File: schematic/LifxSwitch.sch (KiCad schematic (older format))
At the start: 27 parts

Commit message: Completed Schematic
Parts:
- removed C?: 4.7uF, symbol C
- removed L?: 3.3uH, symbol L
- removed R?: 50k, symbol R
- removed R?: 25k, symbol R
- removed U?: ST1S06, symbol ST1S06
- added C1, C3: 4.7uF, symbol C
- added C2, C4: 0.1uF, symbol C
- added D1: SP0503BAHTG, SOT192P237X122-4N, symbol SP0503BAHTG
- added D2, D3: LED, symbol LED
- added J4: CP2102, symbol Conn_01x02
- added J5: Arcade, symbol Conn_01x01
- added R1: 1k, symbol R
- added R2: 22.1k, symbol R
- added R3: 47.5k, symbol R
- added U2: CP2102N-A01-GQFN20, SILABS_QFN20, symbol CP2102N-A01-GQFN20
- gave numbers to parts that had none: 22
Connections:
- net +3V3: now also R4.1, C1.2, C2.2, D2.2 (A), D3.2 (A), R1.1, U2.6 (VDD)
- net +5V: now also C3.2, C4.2, D1.3 (B), R2.1, U2.7 (VREGIN)
- net LightStatus: now also J5.1 (Pin_1)
- net RX: now also U2.18 (TXD)
- net TX: now also U2.17 (RXD)
- net VSS: now also C7.1, C8.1, J3.5 (Shield), C1.1, C2.1, C3.1, C4.1, D1.1 (GND), R3.2, U2.12 (GND), U2.21 (GND), U2.3 (GND)
- net Gpio0: now reaches U3.8 (RDY), U4.12 (GPIO0)
- net at J3.2 (D-): now also D1.2 (A), U2.5 (D)
- net at J3.3 (D+): now also D1.4 (C), U2.4 (D+)
- new net: D2.1 (K), U2.19 (GPIO.3/RXT)
- new net: D3.1 (K), U2.20 (GPIO.2/TXT)
- new net: R2.2, R3.1, U2.8 (VBUS)
- new net: R1.2, U2.9 (RST)
- new net G0: J4.1 (Pin_1), U2.2 (GPIO.0/CLK)
- new net G1: J4.2 (Pin_2), U2.1 (GPIO.1/RS485)
- no-connect marks 2 -> 15
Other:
- moved on the sheet: C5, C6, C7, C8, C9, D4, D5, D6, D7, J3, R10, R4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

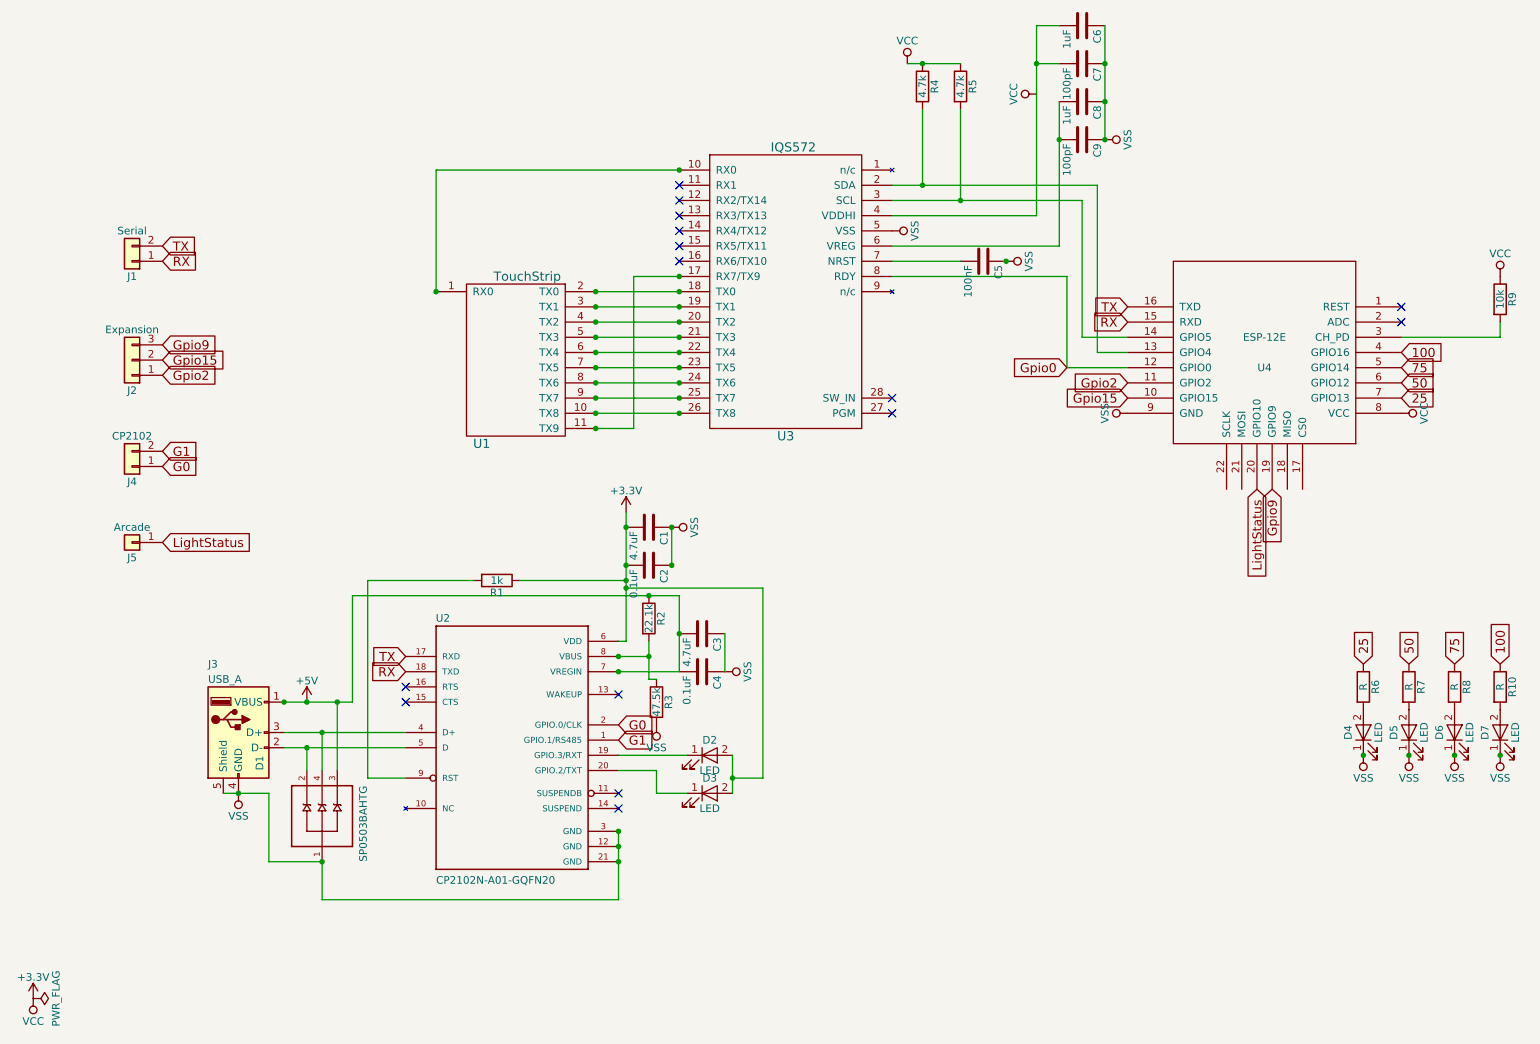
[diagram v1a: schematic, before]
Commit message: Completed PCB layout
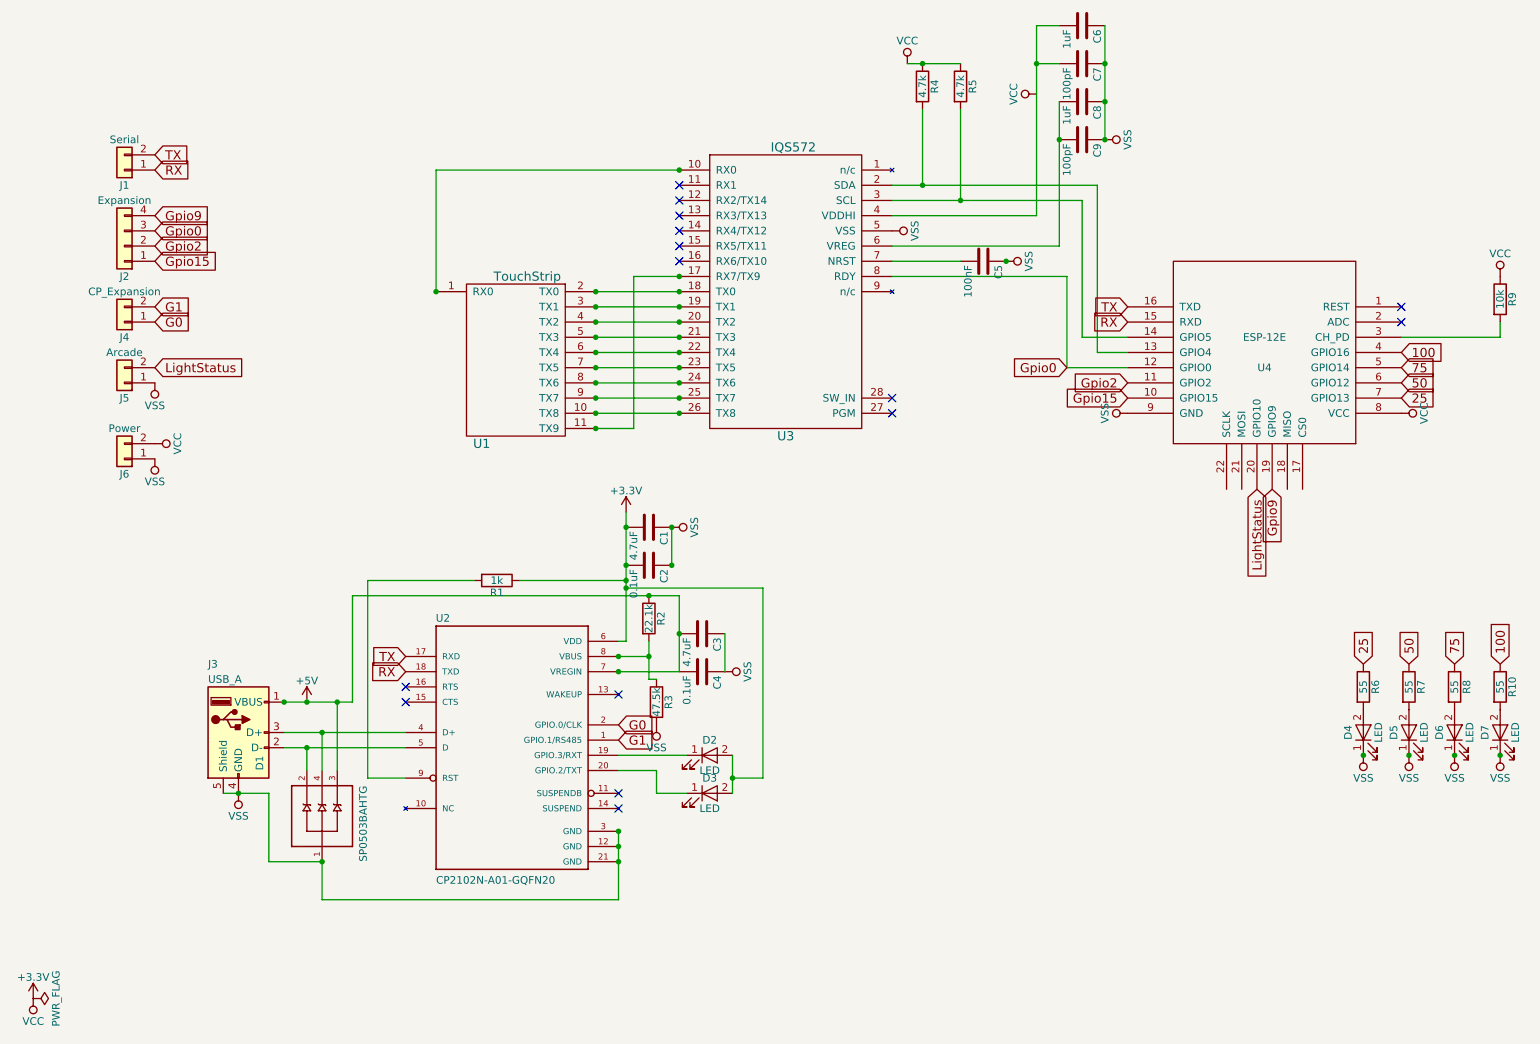
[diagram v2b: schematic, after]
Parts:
- removed J2: Expansion, symbol Conn_01x03
- removed J5: Arcade, symbol Conn_01x01
- added J2: Expansion, Pin_Headers:Pin_Header_Straight_1x04_Pitch2.54mm, symbol Conn_01x04
- added J5: Arcade, Pin_Headers:Pin_Header_Straight_1x02_Pitch2.54mm, symbol Conn_01x02
- added J6: Power, Pin_Headers:Pin_Header_Straight_1x02_Pitch2.54mm, symbol Conn_01x02
- C1, C2, C3, C4, C5, C6, C7, C8, C9: footprint (none) -> Capacitors_SMD:C_0805
- D1: footprint SOT192P237X122-4N -> SP0503BAHTG:SOT192P237X122-4N
- D2, D3, D4, D5, D6, D7: footprint (none) -> LEDs:LED_0805
- J1: footprint (none) -> Pin_Headers:Pin_Header_Straight_1x02_Pitch2.54mm
- J3: footprint (none) -> Connectors_USB:USB_Micro-B_Molex_47346-0001
- J4: value CP2102 -> CP_Expansion; footprint (none) -> Pin_Headers:Pin_Header_Straight_1x02_Pitch2.54mm
- R1, R2, R3, R4, R5, R9: footprint (none) -> Resistors_SMD:R_0805
- R10, R6, R7, R8: value R -> 55; footprint (none) -> Resistors_SMD:R_0805
- U1: footprint (none) -> Buttons_Switches_SMD:Touchstrip
- U2: footprint SILABS_QFN20 -> CP2102N-A01-GQFN20:SILABS_QFN20
- U3: footprint (none) -> Housings_DFN_QFN:QFN-28-1EP_4x4mm_Pitch0.4mm-Without-Center-Pads
- U4: footprint (none) -> ESP8266:ESP-12E
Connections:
- net +3V3: now also J6.2 (Pin_2)
- net Gpio0: now also J2.3 (Pin_3)
- net Gpio15: now also J2.1 (Pin_1)
- net Gpio2: now also J2.2 (Pin_2)
- net Gpio9: now also J2.4 (Pin_4)
- net LightStatus: now also J5.2 (Pin_2)
- net VSS: now also J5.1 (Pin_1), J6.1 (Pin_1)
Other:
- moved on the sheet: J1, J4

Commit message: Finished V1 schematic
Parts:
- removed J5: Arcade, Pin_Headers:Pin_Header_Straight_1x02_Pitch2.54mm, symbol Conn_01x02
- added C10: 10uF, symbol C
- added C11: 0.1uF, symbol C
- added J5: Arcade, Pin_Headers:Pin_Header_Straight_1x04_Pitch2.54mm, symbol Conn_01x04
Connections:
- net +3V3: now also C10.1, C11.1
- net Gpio15: now also J5.3 (Pin_3)
- net LightStatus: now also J5.4 (Pin_4)
- net VSS: now also C10.2, C11.2, J5.1 (Pin_1), J5.2 (Pin_2)
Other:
- moved on the sheet: J6
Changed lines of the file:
@@
 L VCC #PWR09
 U 1 1 5B29EAF7
-P 10050 3300
-F 0 "#PWR09" H 10050 3150 50  0001 C CNN
-F 1 "VCC" H 10050 3450 50  0000 C CNN
-F 2 "" H 10050 3300 50  0001 C CNN
-F 3 "" H 10050 3300 50  0001 C CNN
-	1    10050 3300
+P 10400 3300
+F 0 "#PWR09" H 10400 3150 50  0001 C CNN
+F 1 "VCC" H 10400 3450 50  0000 C CNN
+F 2 "" H 10400 3300 50  0001 C CNN
+F 3 "" H 10400 3300 50  0001 C CNN
+	1    10400 3300
 	0    1    1    0
 $EndComp
@@
 Connection ~ 3700 2500
 Connection ~ 5300 1700
-Text GLabel 1850 3000 2    60   Input ~ 0
+Text GLabel 1850 3500 2    60   Input ~ 0
 LightStatus
 Text GLabel 7850 3000 0    60   Input ~ 0
@@
 Gpio0
 $Comp
-L Conn_01x02 J5
-U 1 1 5B3181C2
-P 1650 3100
-F 0 "J5" H 1650 3200 50  0000 C CNN
-F 1 "Arcade" H 1650 2900 50  0000 C CNN
-F 2 "Pin_Headers:Pin_Header_Straight_1x02_Pitch2.54mm" H 1650 3100 50  0001 C CNN
-F 3 "" H 1650 3100 50  0001 C CNN
-	1    1650 3100
-	-1   0    0    1
-$EndComp
-$Comp
 L VSS #PWR022
 U 1 1 5B318428
-P 1850 3100
-F 0 "#PWR022" H 1850 2950 50  0001 C CNN
-F 1 "VSS" H 1850 3250 50  0000 C CNN
-F 2 "" H 1850 3100 50  0001 C CNN
-F 3 "" H 1850 3100 50  0001 C CNN
-	1    1850 3100
-	-1   0    0    1
+P 1850 3700
+F 0 "#PWR022" H 1850 3550 50  0001 C CNN
+F 1 "VSS" H 1850 3850 50  0000 C CNN
+F 2 "" H 1850 3700 50  0001 C CNN
+F 3 "" H 1850 3700 50  0001 C CNN
+	1    1850 3700
+	0    1    1    0
 $EndComp
 $Comp
 L Conn_01x02 J6
 U 1 1 5B3184A8
-P 1650 3600
-F 0 "J6" H 1650 3700 50  0000 C CNN
-F 1 "Power" H 1650 3400 50  0000 C CNN
-F 2 "Pin_Headers:Pin_Header_Straight_1x02_Pitch2.54mm" H 1650 3600 50  0001 C CNN
-F 3 "" H 1650 3600 50  0001 C CNN
-	1    1650 3600
+P 1650 3150
+F 0 "J6" H 1650 3250 50  0000 C CNN
+F 1 "Power" H 1650 2950 50  0000 C CNN
+F 2 "Pin_Headers:Pin_Header_Straight_1x02_Pitch2.54mm" H 1650 3150 50  0001 C CNN
+F 3 "" H 1650 3150 50  0001 C CNN
+	1    1650 3150
 	-1   0    0    1
 $EndComp
@@
 L VSS #PWR023
 U 1 1 5B3185A5
-P 1850 3600
-F 0 "#PWR023" H 1850 3450 50  0001 C CNN
-F 1 "VSS" H 1850 3750 50  0000 C CNN
-F 2 "" H 1850 3600 50  0001 C CNN
-F 3 "" H 1850 3600 50  0001 C CNN
-	1    1850 3600
+P 1850 3150
+F 0 "#PWR023" H 1850 3000 50  0001 C CNN
+F 1 "VSS" H 1850 3300 50  0000 C CNN
+F 2 "" H 1850 3150 50  0001 C CNN
+F 3 "" H 1850 3150 50  0001 C CNN
+	1    1850 3150
 	-1   0    0    1
 $EndComp
@@
 L VCC #PWR024
 U 1 1 5B318603
-P 1850 3500
-F 0 "#PWR024" H 1850 3350 50  0001 C CNN
-F 1 "VCC" H 1850 3650 50  0000 C CNN
-F 2 "" H 1850 3500 50  0001 C CNN
-F 3 "" H 1850 3500 50  0001 C CNN
-	1    1850 3500
-	0    1    1    0
-$EndComp
+P 1850 3050
+F 0 "#PWR024" H 1850 2900 50  0001 C CNN
+F 1 "VCC" H 1850 3200 50  0000 C CNN
+F 2 "" H 1850 3050 50  0001 C CNN
+F 3 "" H 1850 3050 50  0001 C CNN
+	1    1850 3050
+	0    1    1    0
+$EndComp
+$Comp
+L Conn_01x04 J5
+U 1 1 5B323DF4
+P 1650 3700
+F 0 "J5" H 1650 3900 50  0000 C CNN
+F 1 "Arcade" H 1650 3400 50  0000 C CNN
+F 2 "Pin_Headers:Pin_Header_Straight_1x04_Pitch2.54mm" H 1650 3700 50  0001 C CNN
+F 3 "" H 1650 3700 50  0001 C CNN
+	1    1650 3700
+	-1   0    0    1
+$EndComp
+Text GLabel 1850 3600 2    60   Input ~ 0
+Gpio15
+$Comp
+L VSS #PWR025
+U 1 1 5B3241F7
+P 1850 3800
+F 0 "#PWR025" H 1850 3650 50  0001 C CNN
+F 1 "VSS" H 1850 3950 50  0000 C CNN
+F 2 "" H 1850 3800 50  0001 C CNN
+F 3 "" H 1850 3800 50  0001 C CNN
+	1    1850 3800
+	0    1    1    0
+$EndComp
+Wire Wire Line
+	10050 3300 10400 3300
+$Comp
+L C C11
+U 1 1 5B35919E
+P 10350 3450
+F 0 "C11" H 10375 3550 50  0000 L CNN
+F 1 "0.1uF" H 10375 3350 50  0000 L CNN
+F 2 "" H 10388 3300 50  0001 C CNN
+F 3 "" H 10350 3450 50  0001 C CNN
+	1    10350 3450
+	1    0    0    -1
+$EndComp
+$Comp
+L C C10
+U 1 1 5B359203
+P 10100 3450
+F 0 "C10" H 10125 3550 50  0000 L CNN
+F 1 "10uF" H 10125 3350 50  0000 L CNN
+F 2 "" H 10138 3300 50  0001 C CNN
+F 3 "" H 10100 3450 50  0001 C CNN
+	1    10100 3450
+	1    0    0    -1
+$EndComp
+Wire Wire Line
+	10100 3600 10350 3600
+$Comp
+L VSS #PWR026
+U 1 1 5B3595DA
+P 10250 3600
+F 0 "#PWR026" H 10250 3450 50  0001 C CNN
+F 1 "VSS" H 10250 3750 50  0000 C CNN
+F 2 "" H 10250 3600 50  0001 C CNN
+F 3 "" H 10250 3600 50  0001 C CNN
+	1    10250 3600
+	-1   0    0    1
+$EndComp
+Connection ~ 10100 3300
+Connection ~ 10350 3300
+Connection ~ 10250 3600
 $EndSCHEMATC

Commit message: Finished V1 schematic
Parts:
- C10, C11: footprint (none) -> Capacitors_SMD:C_0805
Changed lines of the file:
@@
 F 0 "C11" H 10375 3550 50  0000 L CNN
 F 1 "0.1uF" H 10375 3350 50  0000 L CNN
-F 2 "" H 10388 3300 50  0001 C CNN
+F 2 "Capacitors_SMD:C_0805" H 10388 3300 50  0001 C CNN
 F 3 "" H 10350 3450 50  0001 C CNN
 	1    10350 3450
@@
 F 0 "C10" H 10125 3550 50  0000 L CNN
 F 1 "10uF" H 10125 3350 50  0000 L CNN
-F 2 "" H 10138 3300 50  0001 C CNN
+F 2 "Capacitors_SMD:C_0805" H 10138 3300 50  0001 C CNN
 F 3 "" H 10100 3450 50  0001 C CNN
 	1    10100 3450

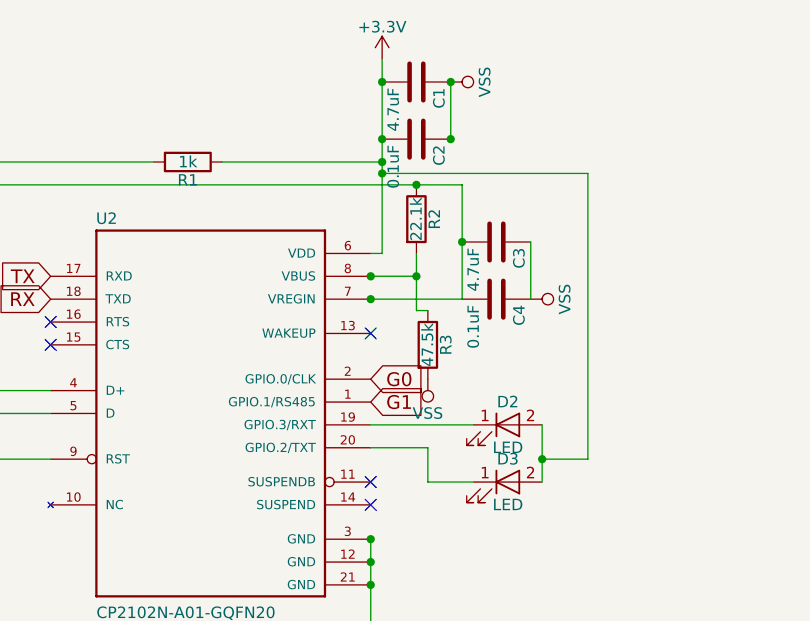
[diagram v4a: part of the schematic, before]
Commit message: Fixed dimmer footprint
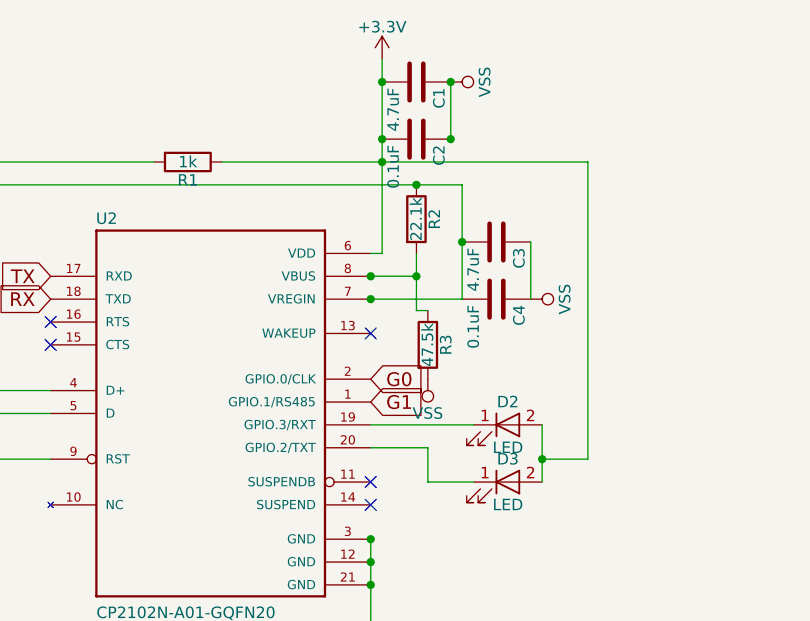
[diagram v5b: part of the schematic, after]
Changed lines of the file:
@@
 $EndComp
 Wire Wire Line
-	4250 4400 4950 4400
+	4250 4400 5850 4400
 Connection ~ 4950 4400
 Wire Wire Line
@@
 	5650 5550 5650 5800
 Wire Wire Line
-	4950 4450 5850 4450
-Wire Wire Line
-	5850 4450 5850 5700
+	5850 4400 5850 5700
 Wire Wire Line
 	5850 5700 5650 5700
 Connection ~ 5650 5700
-Connection ~ 4950 4450
 Text GLabel 3500 4900 0    60   Input ~ 0
 TX
